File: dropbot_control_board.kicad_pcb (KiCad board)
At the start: 4 copper layers, 115 x 92 mm, 141 parts, among them P1 CONN_01X01, P10 CONN_01X01, P11 TFM-105-02-X-DH, P2 CONN_01X01, P3 CONN_01X03, P4 CONN_01X02, P5 CONN_01X01, P6 USB_B, P7 CONN_01X04, P8 CONN_01X03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

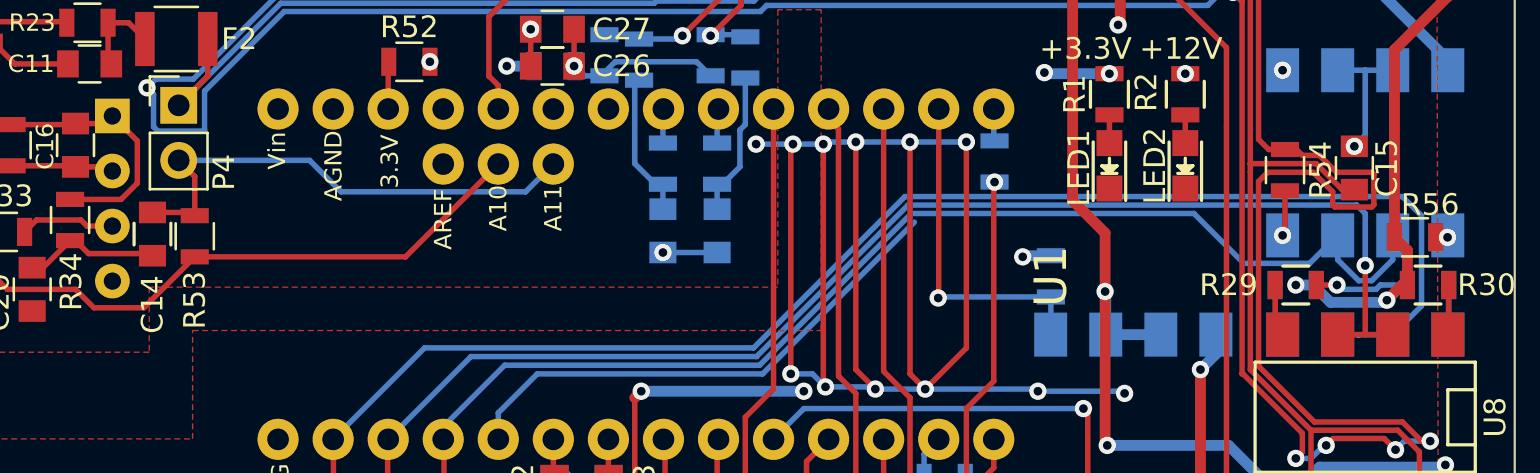
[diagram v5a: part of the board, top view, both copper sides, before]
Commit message: Add missing schematic diagrams and change some part numbers
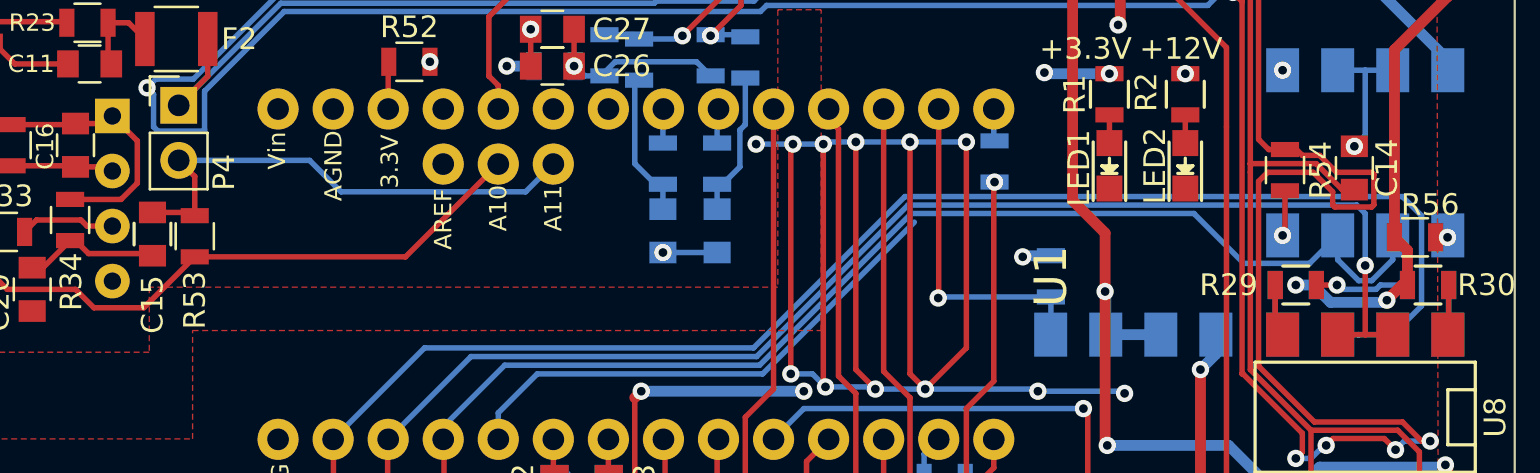
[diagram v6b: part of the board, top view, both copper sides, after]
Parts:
- C12: value 1pF -> 10pF
- C13: value 10pF -> 100pF
- C14: renamed from C15; value 100pF -> 470pF
- R14: value 5.1 -> 1
- renumbered C14 to C15
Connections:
- net D3 renamed Net-(U1-Pad3)

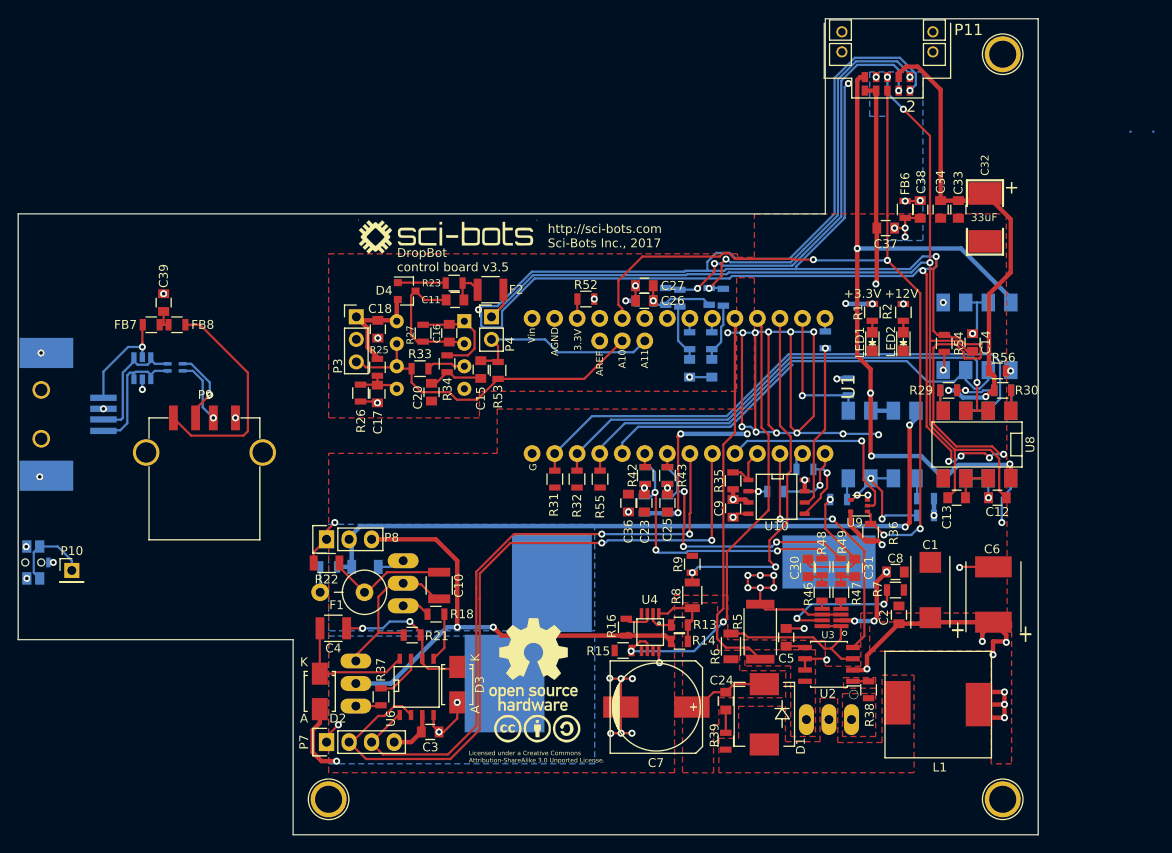
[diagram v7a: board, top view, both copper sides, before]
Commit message: Improve layout/stability of boost converter, etc.
* improve layout/stability of boost converter
* enable on board calibration without HVOE
* add decoupling cap to 0.6V reference
* fix footprint for U10
* add programming wire
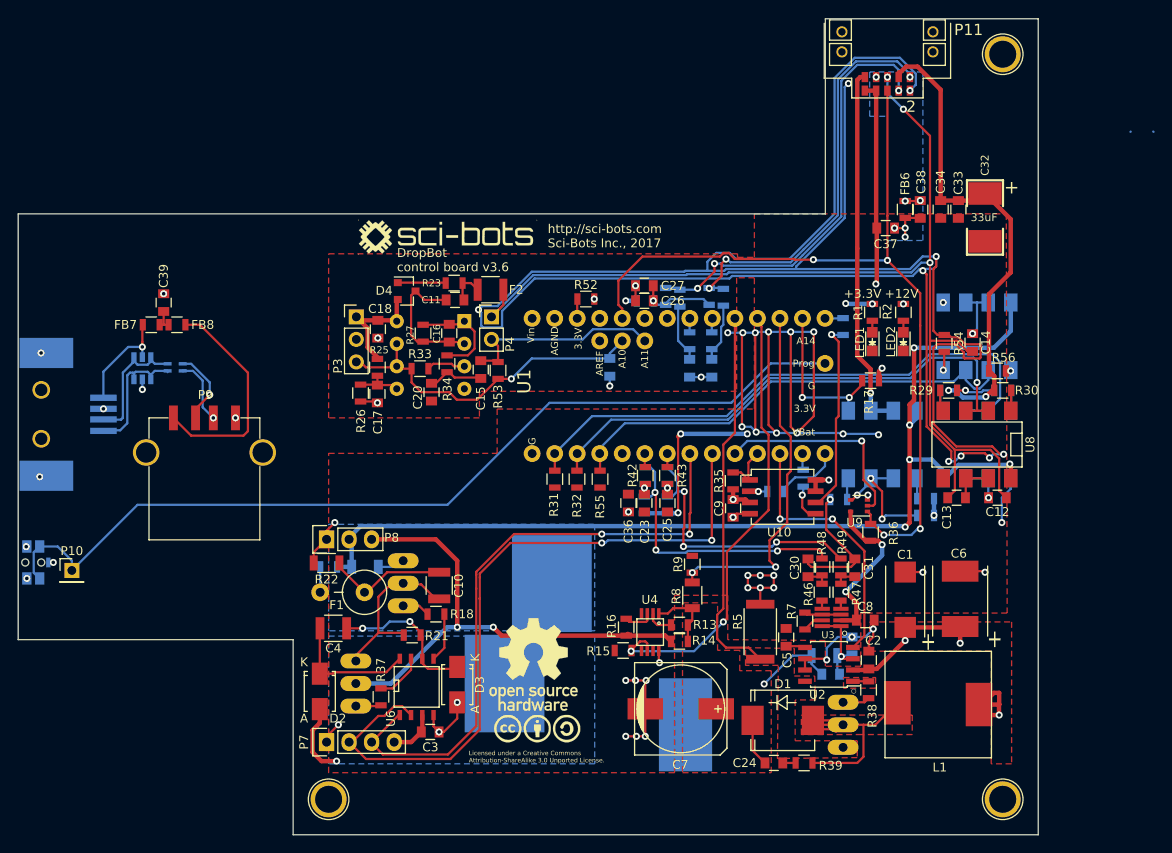
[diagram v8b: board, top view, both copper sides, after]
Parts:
- added C19: 100pF, Capacitors_SMD:C_0805, B.Cu at (124.6, 94.9)
- added C21: 100pF, Capacitors_SMD:C_0805, B.Cu at (127.0, 91.7)
- added C22: 0.1uF, Capacitors_SMD:C_0805, B.Cu at (99.7, 60.3)
- D5: footprint wurth-WE-TVS_SOT23-6L -> WheelerLab:wurth-WE-TVS_SOT23-6L
- L2: footprint wurth-WE-CNSW_0805 -> WheelerLab:wurth-WE-CNSW_0805
- R11, R12, R24, R28, R29, R30, R54, R56: value 200 -> 150
- R17: moved to F.Cu
- R6: moved to B.Cu
- U1: footprint footprints:Teensy-3.2 -> WheelerLab:Teensy-3.2
- U10: footprint SMD_Packages:SOIC-8-N -> SSO-8_5.2x5.2mm_Pitch1.27mm
- moved R7 10.8 mm to (121.7, 88.9), turned to 90 degrees
- moved R6 10.6 mm to (123.9, 92.8), turned to 0 degrees
- moved R39 9.16 mm to (121.6, 104.9), turned to 0 degrees
- moved C24 8.84 mm to (118.2, 104.9), turned to 0 degrees
- moved C8 6.40 mm to (128.5, 88.8)
- moved C2 6.13 mm to (128.9, 93.3)
- moved C6 3.78 mm to (139.2, 86.4)
- moved C1 3.04 mm to (133.0, 86.5)
- moved C7 2.76 mm to (107.7, 98.8)
- moved R17 2.60 mm to (129.1, 61.8), turned to 180 degrees
- moved FB5 2.50 mm to (126.0, 55.7)
- moved D1 2.18 mm to (119.2, 100.1), turned to 0 degrees
- moved Q1 1.70 mm to (126.0, 100.6), turned to 270 degrees
- moved FB4 1.02 mm to (121.5, 72.8), turned to 90 degrees
- moved U10 0.70 mm to (119.2, 74.9), turned to 0 degrees
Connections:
- P10 pad 1: Net-(P10-Pad1) -> PROG
- SW1 pad 1: Net-(P10-Pad1) -> PROG
- U12 pad 8: VOUT -> HVAC
- U7 pad 8: VOUT -> HVAC
- U8 pad 8: VOUT -> HVAC
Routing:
- net PROG: track 0.00 -> 104.3 mm
- net VOUT: track 89.0 -> 41.5 mm, vias 4 -> 1
- net HVAC: track 82.0 -> 122.6 mm, vias 2 -> 5
- net Net-(D1-Pad2): track 0.75 -> 28.2 mm
- net Net-(U1-Pad3): track 24.1 -> 0.00 mm
- net +12V: track 79.7 -> 66.0 mm, vias 10 -> 6
- net Net-(R7-Pad1): track 15.1 -> 2.37 mm, vias 2 -> 0
- net Net-(P10-Pad1): track 9.68 -> 0.00 mm
- net Net-(C19-Pad1): track 20.0 -> 11.7 mm, vias 0 -> 1
- net Net-(C19-Pad2): track 16.5 -> 22.7 mm, vias 0 -> 1
- net GND: track 359.1 -> 364.5 mm, vias 44 -> 47
- net +3.3V: track 116.2 -> 120.2 mm, vias 18 -> 16
- net D11/M0SI: track 7.59 -> 4.18 mm
- net D13/CLK: track 18.6 -> 21.9 mm
- net Net-(Q1-Pad1): track 0.00 -> 3.07 mm
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- removed copper zone on F.Cu, net Net-(Q1-Pad1)
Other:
- board text added: "DropBot control board v3.6"
- board text removed: "DropBot control board v3.5"
